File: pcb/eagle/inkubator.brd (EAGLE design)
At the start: 71.1 x 50.5 mm, 34 parts, among them Q1 BT138-600, Q2 BT138-600, U1 L78L33ABUTR, U2 MOC3063, U3 MOC3063

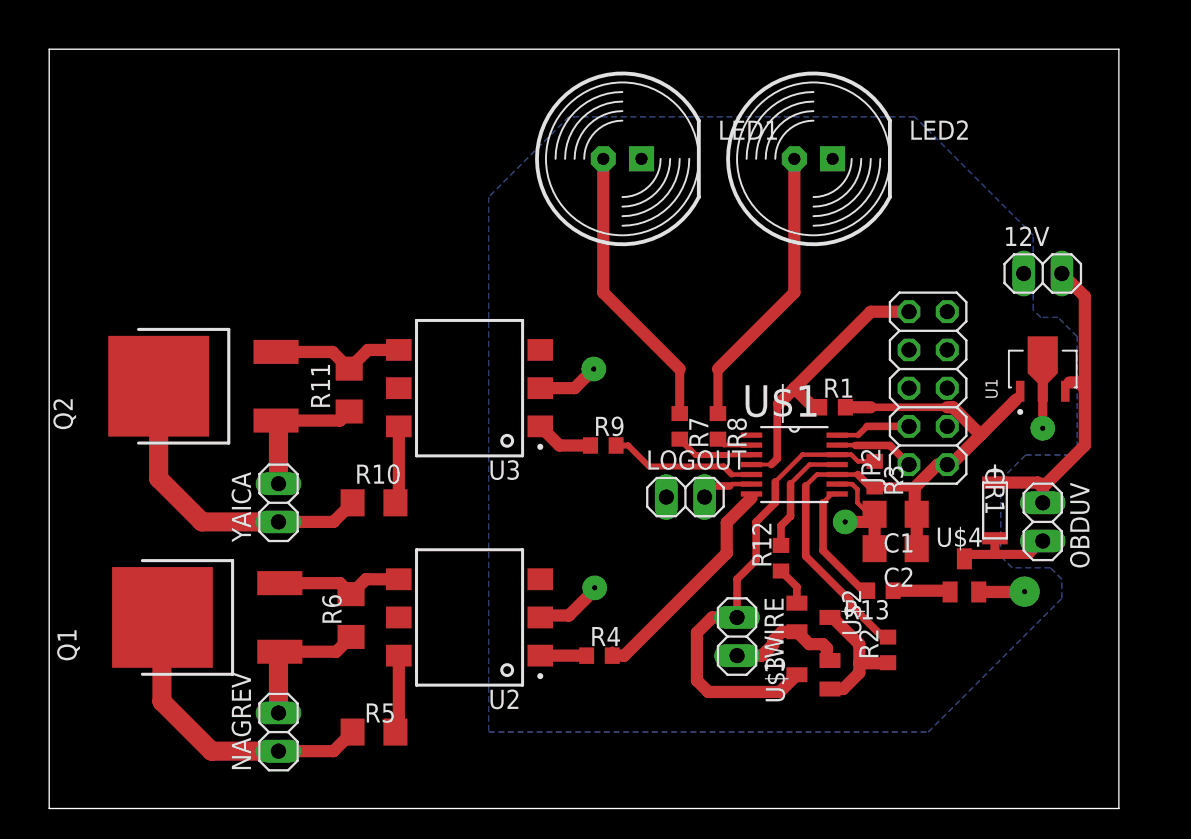
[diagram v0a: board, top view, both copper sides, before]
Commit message: Рефакторинг принципиальной схемы и печатной платы
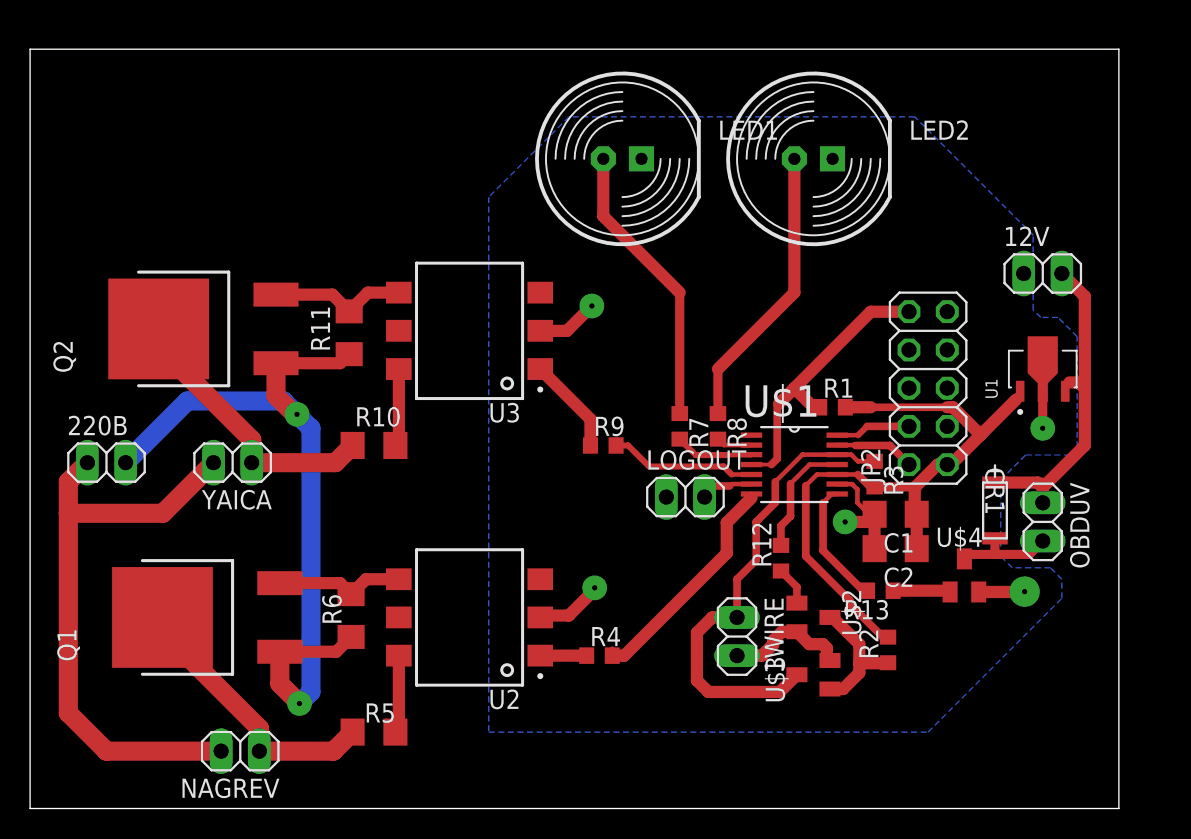
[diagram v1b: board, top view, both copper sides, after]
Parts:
- added 220В: (no value), pinhead:1X02
- moved YAICA 4.05 mm to (13.5, 23.0), turned to 180 degrees
- moved R11 3.81 mm to (21.2, 31.6)
- moved Q2 3.81 mm to (12.4, 31.9)
- moved R10 3.81 mm to (22.9, 24.1)
- moved U3 3.81 mm to (29.2, 31.8)
- moved NAGREV 2.84 mm to (14.0, 3.81), turned to 180 degrees
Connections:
- net N$13: now also 220В.2, Q1.1, R6.1; no longer YAICA.2
- net N$6: now also 220В.1, YAICA.2; no longer Q1.1, R6.1
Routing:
- net N$13: track 9.38 -> 52.1 mm, vias 0 -> 2
- net N$6: track 9.25 -> 39.4 mm
- net N$7: track 3.87 -> 6.46 mm
- net N$12: track 20.7 -> 19.0 mm
- net N$5: track 20.8 -> 19.6 mm
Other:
- board size 71.1 x 50.5 mm -> 72.4 x 50.5 mm

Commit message: Добавлен узел управления 12-и вольтовым мотором привода яйцекрутилки, для случая если мотор DC 12V
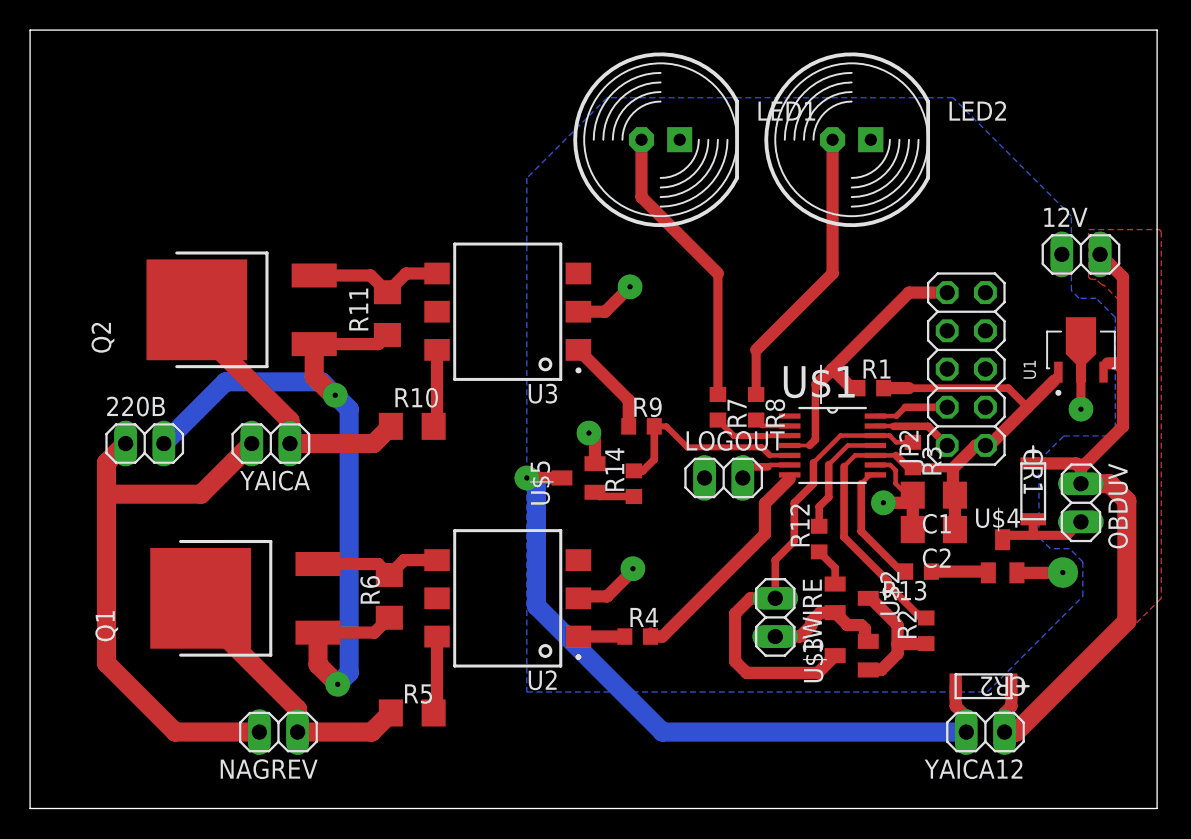
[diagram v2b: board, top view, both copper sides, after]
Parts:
- added CR2: BAS32L,115, BAS32L_115:SOD80C
- added R14: 200, resistor:R0603
- added U$5: IRLML0060, 2n7002:SOT23
- added YAICA12: (no value), pinhead:1X02
- U$4: value 2N7002SO23 -> IRLML0060
- moved R4 2.84 mm to (40.4, 11.4)
- moved U$1 2.84 mm to (53.3, 24.1)
- moved R6 2.84 mm to (23.9, 14.1)
- moved Q1 2.84 mm to (15.2, 14.0)
- moved 220В 2.84 mm to (7.62, 24.3)
- moved NAGREV 2.84 mm to (16.5, 5.08)
- moved Q2 2.84 mm to (15.0, 33.1)
- moved C2 2.84 mm to (60.1, 18.5)
- moved LED1 2.84 mm to (41.9, 44.5)
- moved LED2 2.84 mm to (54.6, 44.5)
- moved R7 2.84 mm to (45.7, 26.7)
- moved R8 2.84 mm to (48.3, 26.7)
- moved U3 2.84 mm to (31.8, 33.0)
- moved YAICA 2.84 mm to (16.0, 24.3)
- moved U$2 2.84 mm to (54.6, 14.0)
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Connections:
- new net N$17: R14.1, U$5.1
- new net N$18: CR2.2, U$5.3, YAICA12.2
- net +12V: now also CR2.1, YAICA12.1
- net GND: now also U$5.2
- net YAICA: now also R14.2
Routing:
- net N$18: track 0.00 -> 46.5 mm, vias 0 -> 1
- net +12V: track 22.5 -> 48.4 mm
- net YAICA: track 9.80 -> 13.7 mm
- net N$17: track 0.00 -> 2.70 mm
- net GND: track 30.9 -> 33.2 mm, vias 5 -> 6
- net N$6: track 39.4 -> 38.2 mm
- added copper zone on layer 1, net +12V
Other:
- board size 72.4 x 50.5 mm -> 74.9 x 51.7 mm
